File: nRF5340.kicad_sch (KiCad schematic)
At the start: 33 parts, among them SW1 BGS12P2L6, U2 nRF5340-CLXX

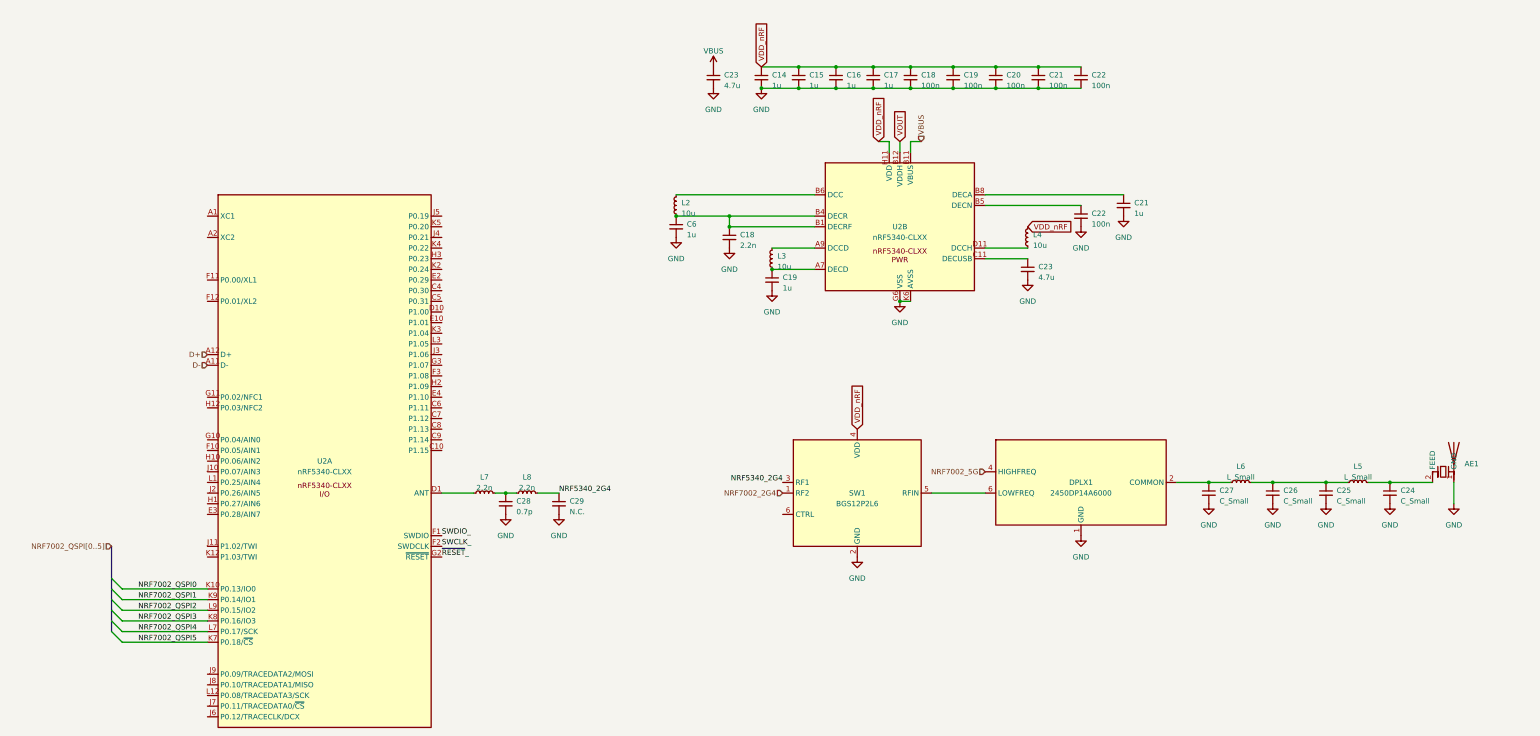
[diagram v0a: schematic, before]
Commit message: Added passvies and bus connections to nRF7002
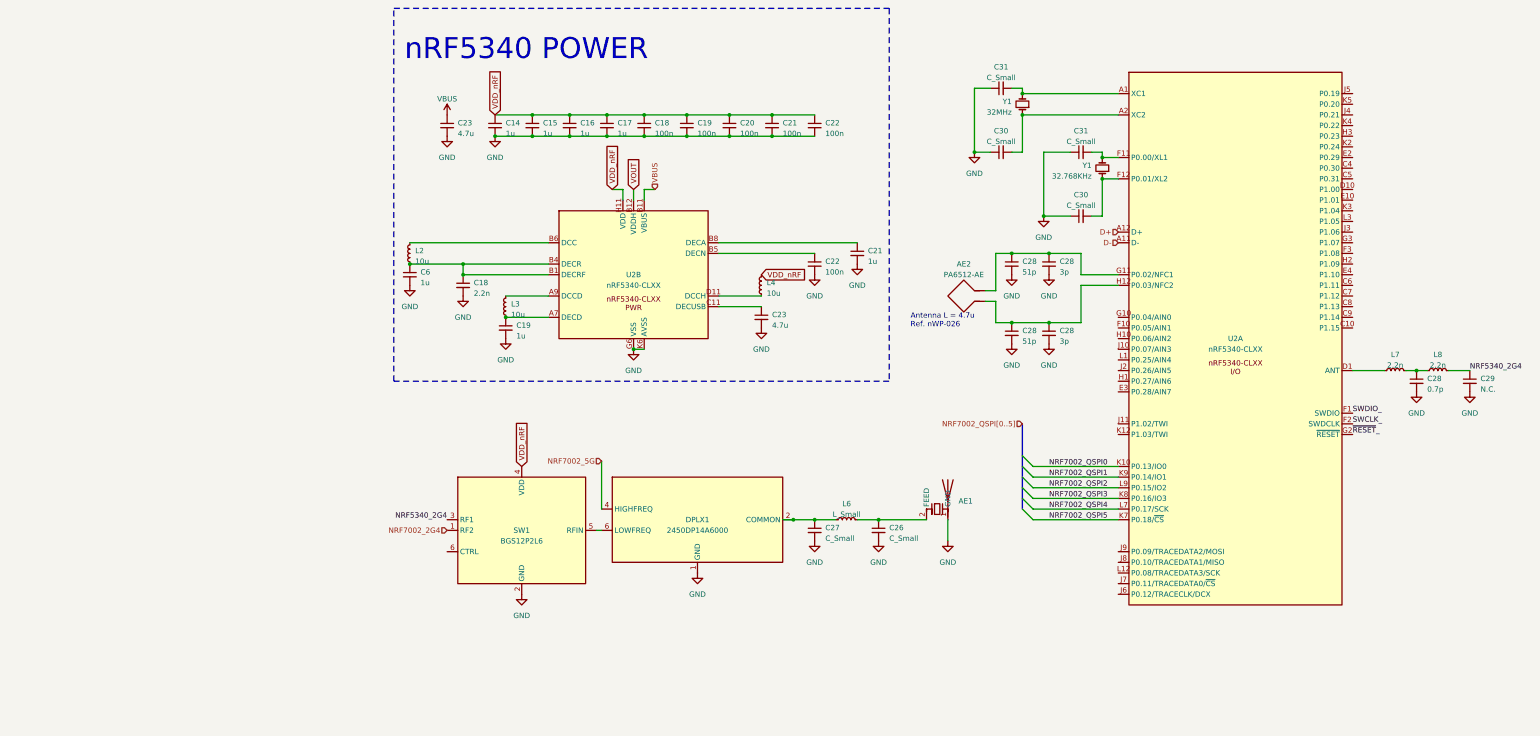
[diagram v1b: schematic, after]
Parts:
- removed C24, C25: C_Small, symbol Device:C_Small
- removed L5: L_Small, symbol Device:L_Small
- added AE2: PA6512-AE, symbol Device:Antenna_Loop
- added C28 (x2): 3p, symbol Device:C_Small
- added C28 (x2): 51p, symbol Device:C_Small
- added C30 (x2), C31 (x2): C_Small, symbol Device:C_Small
- added Y1: 32MHz, symbol Device:Crystal_Small
- added Y1: 32.768KHz, symbol Device:Crystal_Small
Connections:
- net GND: now also C28.2, C28.2, C28.2, C28.2, C30.1, C30.1, C31.1, C31.1
- net at U2.A1 (XC1): now also C31.2, Y1.2
- net at U2.A2 (XC2): now also C30.2, Y1.1
- net at U2.F11 (P0.00/XL1): now also C31.2, Y1.2
- net at U2.F12 (P0.01/XL2): now also C30.2, Y1.1
- net at U2.G11 (P0.02/NFC1): now also AE2.2, C28.1, C28.1
- net at U2.H12 (P0.03/NFC2): now also AE2.1, C28.1, C28.1
- net at C26.1, L6.2: now also AE1.2 (FEED)
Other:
- note added: "Antenna L = 4.7u Ref. nWP-026"
- note added: "nRF5340 POWER"
- moved on the sheet: AE1, C14, C15, C16, C17, C18, C19, C20, C21, C22, C23, C26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

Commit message: Schematic complete.
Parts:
- removed AE2: PA6512-AE, symbol Device:Antenna_Loop
- removed C28 (x2): 3p, symbol Device:C_Small
- removed C28 (x2): 51p, symbol Device:C_Small
- removed DPLX1: 2450DP14A6000, rf-lib:2450DP14A6000, symbol rf-lib:2450DP14A6000
- removed L4: 10u, symbol Device:L_Small
- added DPLX1: DPX105950DT-6112A2, rf-lib:DPX105950DT-6112A2, symbol rf-lib:DPX105950DT-6112A2
- added R3, R4, R5, R6: 5.1k, Resistor_SMD:R_0603_1608Metric, symbol Device:R_Small_US
- AE1: value ~ -> Capacitor_SMD:C_0402_1005Metric; MPN (none) -> 2450AD14A5500
- C14, C15, C16, C17, C19, C21, C23, C6: footprint (none) -> Capacitor_SMD:C_0402_1005Metric
- C18, C19, C20, C21, C22, C26, C27, C28, C29: footprint (none) -> Capacitor_SMD:C_0201_0603Metric
- C30, C31: value C_Small -> 8p; footprint (none) -> Capacitor_SMD:C_0201_0603Metric
- L2, L3: footprint (none) -> Inductor_SMD:L_0603_1608Metric
- L6: value L_Small -> 3.3u; footprint (none) -> Inductor_SMD:L_0201_0603Metric
- L7, L8: footprint (none) -> Inductor_SMD:L_0201_0603Metric
- Y1: footprint (none) -> Crystal:Crystal_SMD_2016-4Pin_2.0x1.6mm; symbol Device:Crystal_Small -> Device:Crystal_GND24_Small; MPN (none) -> XRCGB32M000F1S1AR0
- Y1: footprint (none) -> Crystal:Crystal_SMD_3215-2Pin_3.2x1.5mm; MPN (none) -> ECS-.327-6-12-TR9
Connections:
- net VOUT is gone; now on net +3V3: U2.B12 (VDDH)
- net GND: now also Y1.2, Y1.4, DPLX1.1 (GND)
- net NRF5340_2G4: now also SW1.1 (RF2); no longer SW1.3 (RF1)
- net NRF7002_2G4: now also SW1.3 (RF1); no longer SW1.1 (RF2)
- net NRF7002_5G: now also DPLX1.4 (HIGHFREQ)
- net at C27.1, L6.1: now also DPLX1.2 (COMMON)
- net at SW1.5 (RFIN): now also DPLX1.3 (LOWFREQ)
- net at C31.2, U2.A1 (XC1): now also Y1.3; no longer Y1.2
- net ANT_CTRL: now reaches U2.C10 (P1.15)
- net ANT_CTRL: now also SW1.6 (CTRL)
- net OUT0: now reaches U2.C4 (P0.30)
- net OUT1: now reaches U2.C5 (P0.31)
- net NRF7002_CTRL3: now reaches U2.C6 (P1.11)
- net NRF7002_CTRL4: now reaches U2.C7 (P1.12)
- net NRF7002_CTRL5: now reaches U2.C8 (P1.13)
- net NRF7002_CTRL6: now reaches U2.C9 (P1.14)
- net OUT2: now reaches U2.D10 (P1.00)
- net OUT3: now reaches U2.E10 (P1.01)
- net OUT_UART1: now reaches U2.E2 (P0.29)
- net SD_INSERTED: now reaches U2.E3 (P0.28/AIN7)
- net NRF7002_CTRL2: now reaches U2.E4 (P1.10)
- net AIN1: now reaches U2.F10 (P0.05/AIN1)
- net NRF7002_CTRL0: now reaches U2.F3 (P1.08)
- net AIN0: now reaches U2.G10 (P0.04/AIN0)
- net OUT7: now reaches U2.G3 (P1.07)
- net SD_ENABLE: now reaches U2.H1 (P0.27/AIN6)
- net AIN2: now reaches U2.H10 (P0.06/AIN2)
- net NRF7002_CTRL1: now reaches U2.H2 (P1.09)
- net SDA: now reaches U2.H3 (P0.23)
- net SDA: now also R4.2
- net AIN3: now reaches U2.J10 (P0.07/AIN3)
- net OUT_TWI0: now reaches U2.J11 (P1.02/TWI)
- net OUT_TWI0: now also R5.2
- net AIN5: now reaches U2.J2 (P0.26/AIN5)
- net OUT6: now reaches U2.J3 (P1.06)
- net OUT_SPI2: now reaches U2.J4 (P0.21)
- net OUT_SPI0: now reaches U2.J5 (P0.19)
- net FLASH_SD_CTRL4: now reaches U2.J6 (P0.12/TRACECLK/DCX)
- net FLASH_SD_CTRL0: now reaches U2.J7 (P0.11/TRACEDATA0/~{CS})
- net FLASH_SD_CTRL3: now reaches U2.J8 (P0.10/TRACEDATA1/MISO)
- net FLASH_SD_CTRL2: now reaches U2.J9 (P0.09/TRACEDATA2/MOSI)
- net OUT_TWI1: now reaches U2.K12 (P1.03/TWI)
- net OUT_TWI1: now also R6.2
- net OUT_UART0: now reaches U2.K2 (P0.24)
- net OUT4: now reaches U2.K3 (P1.04)
- net SCL: now reaches U2.K4 (P0.22)
- net SCL: now also R3.2
- net OUT_SPI1: now reaches U2.K5 (P0.20)
- net AIN4: now reaches U2.L1 (P0.25/AIN4)
- net FLASH_SD_CTRL1: now reaches U2.L12 (P0.08/TRACEDATA3/SCK)
- net OUT5: now reaches U2.L3 (P1.05)
- net SWCLK_ renamed SWDCLK
- net SWDIO_ renamed SWDIO
- net VDD_nRF renamed +3V3
- net +3V3: now also R3.1, R4.1, R5.1, R6.1
- net ~{RESET}_ renamed ~{RESET}
- no-connect marks 0 -> 3
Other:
- note removed: "Antenna L = 4.7u Ref. nWP-026"
- moved on the sheet: AE1, C14, C15, C16, C17, C18, C19, C20, C21, C22, C23, C26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
